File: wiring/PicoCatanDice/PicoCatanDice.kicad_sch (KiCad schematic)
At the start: 23 parts, among them J1 LCD, J2 SD, Q1 A04407A, SW1 RotaryEncoder_Switch, U1 Pico, U2 NS8002

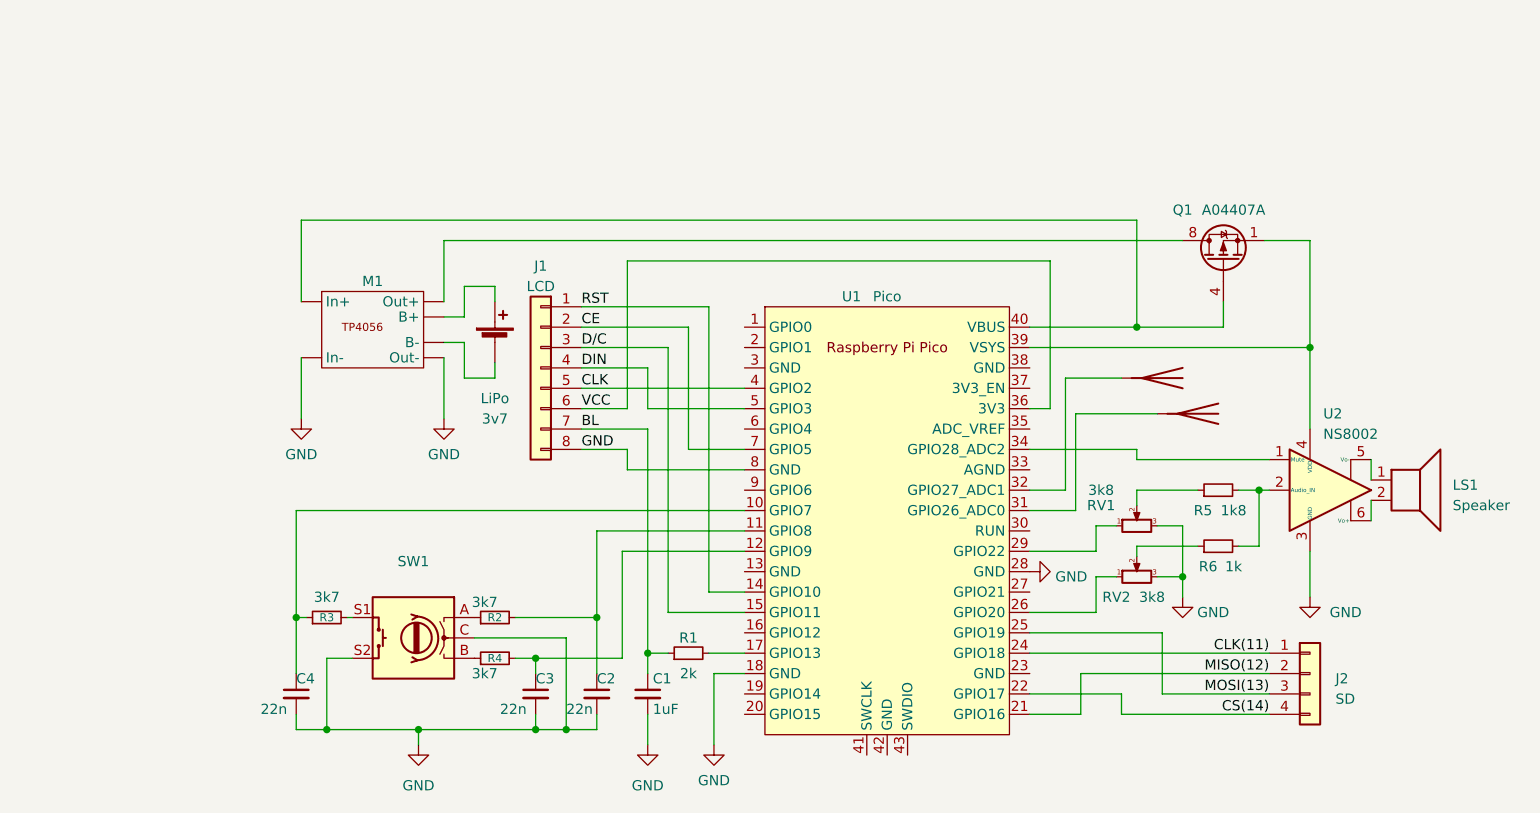
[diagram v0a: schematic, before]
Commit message: 3D enclusure updates
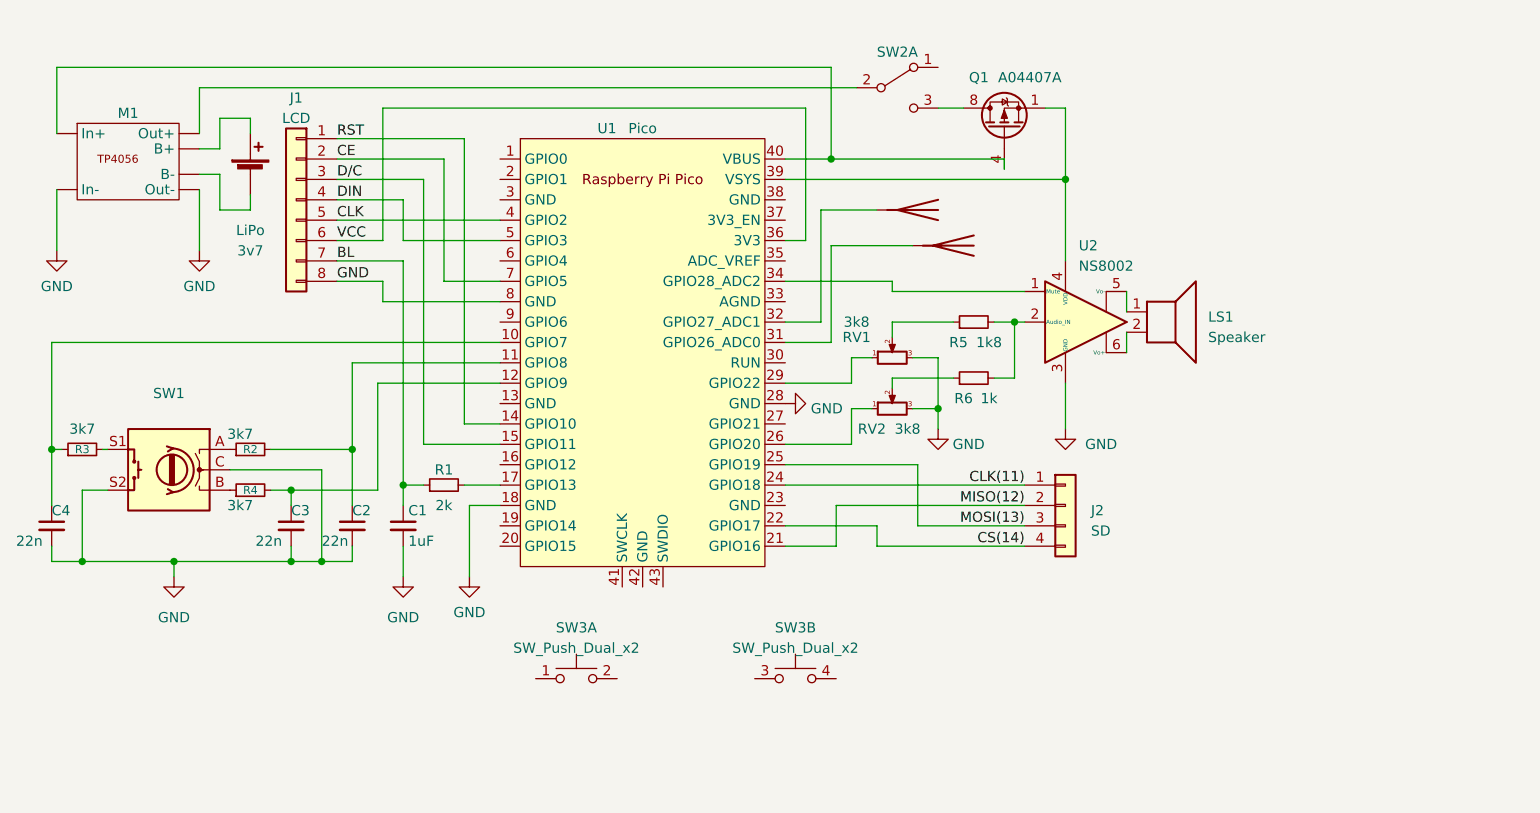
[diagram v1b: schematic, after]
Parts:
- added SW2: SW_DPDT_x2, symbol Switch:SW_DPDT_x2
- added SW3: SW_Push_Dual_x2, symbol Switch:SW_Push_Dual_x2
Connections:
- net at Q1.5 (D), Q1.6 (D), Q1.7 (D)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: now also SW2.3 (C); no longer M1. (Out-)
- new net: M1. (Out-), SW2.2 (B)
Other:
- moved on the sheet: C1, C2, C3, C4, J1, J2, LS1, LiPo, M1, Q1, R1, R2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

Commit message: Added battery check
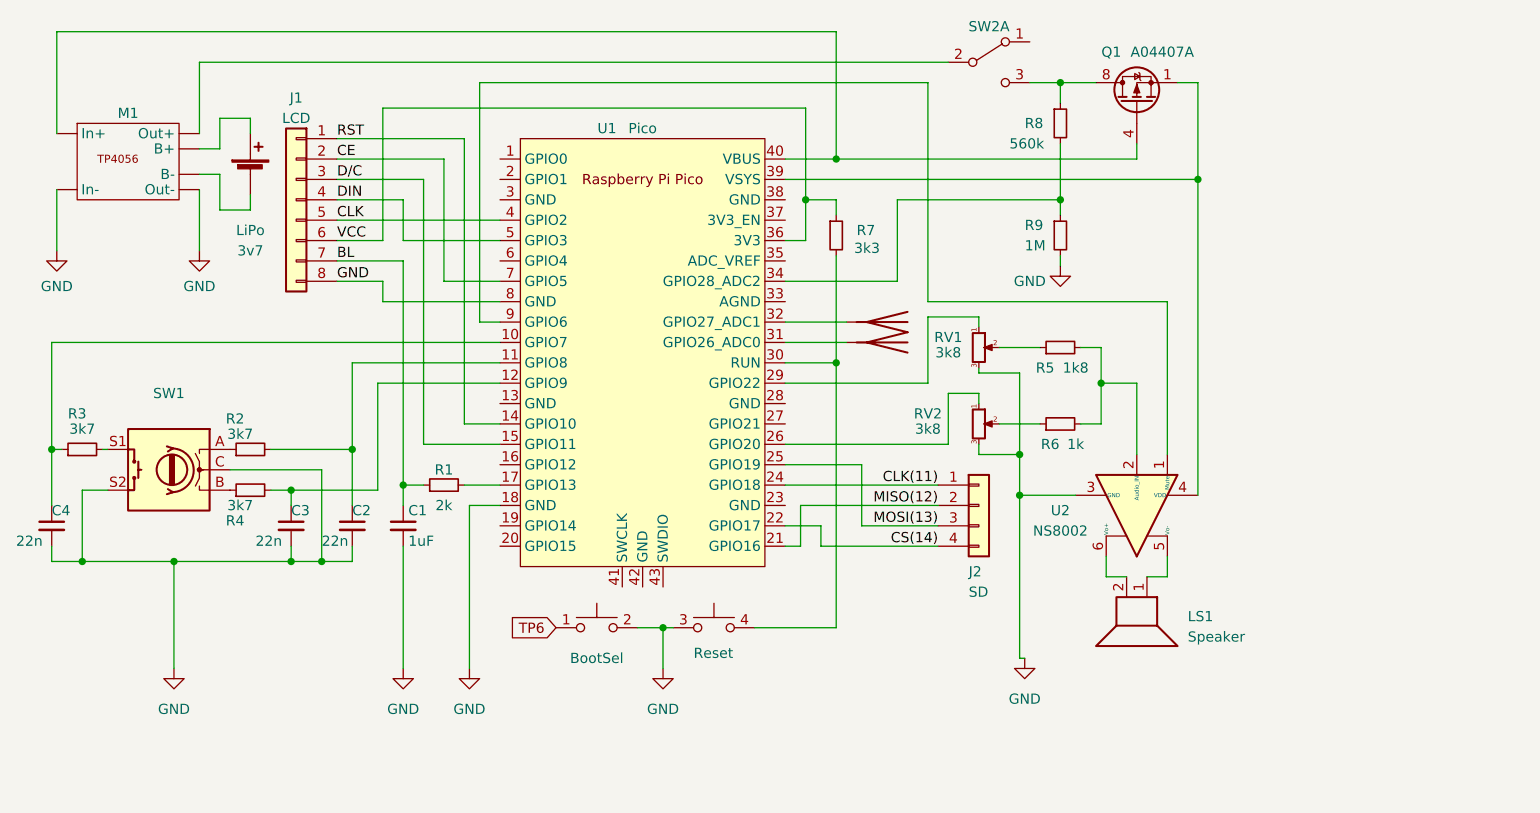
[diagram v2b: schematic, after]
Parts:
- added R7: 3k3, symbol Device:R_Small
- added R8: 560k, symbol Device:R_Small
- added R9: 1M, symbol Device:R_Small
- SW: renamed from SW3; value SW_Push_Dual_x2 -> Reset
- SW3: value SW_Push_Dual_x2 -> BootSel
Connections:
- net GND: now also SW.3 (C), SW3.2 (D), R9.2; no longer U1.28 (GND)
- net VCC: now also R7.1
- net at Q1.5 (D), Q1.6 (D), Q1.7 (D)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: now also R8.1
- net at SW.4 (D): now also U1.30 (RUN), R7.2
- net TP6: now reaches SW3.1 (C)
- net at U1.34 (GPIO28_ADC2): now also R8.2, R9.1; no longer U2.1 (Mute)
- net at U1.9 (GPIO6): now also U2.1 (Mute)
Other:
- moved on the sheet: J2, LS1, Q1, R5, R6, RV1, RV2, SW2A, U2
